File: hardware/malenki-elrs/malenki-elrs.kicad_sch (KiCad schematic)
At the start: 34 parts, among them J1 Conn_01x02_Male-Connector, J2 PROG Header, J3 Weapons, U1 SPX3819M5-L-3-3, U2 ESP32-C3FH4, Y1 ECS-400-10-37B2-CKY-TR

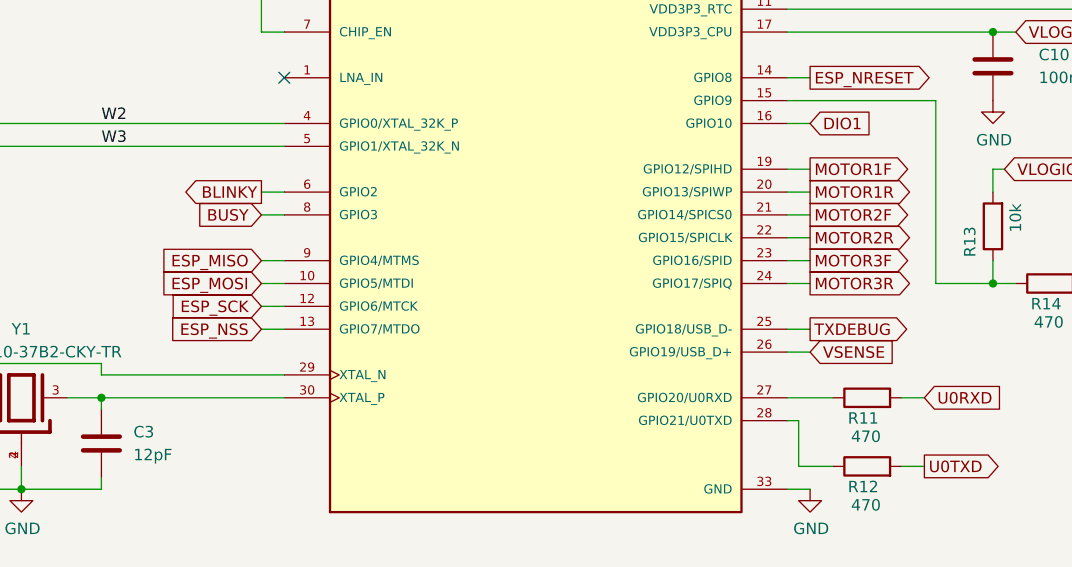
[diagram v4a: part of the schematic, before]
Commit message: Adding ESP32-U4WDH
Found that not enough pins were usable on the esp32-c4 as the internal flash memory still using the SPI bus pins available which I did not initially know about :(
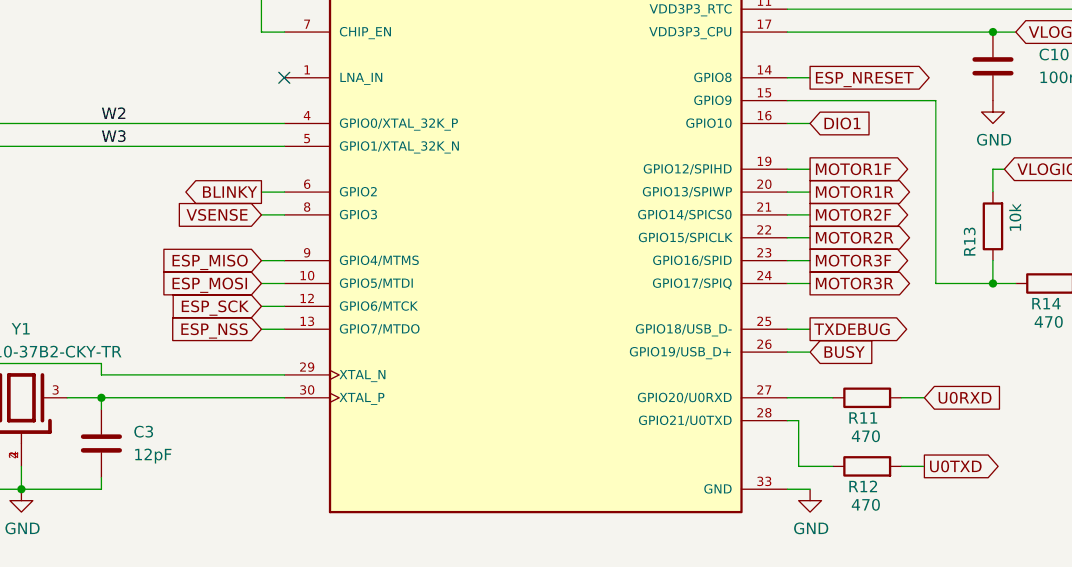
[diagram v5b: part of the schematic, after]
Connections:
- net BUSY: now also U2.26 (GPIO19/USB_D+); no longer U2.8 (GPIO3)
- net VSENSE: now also U2.8 (GPIO3); no longer U2.26 (GPIO19/USB_D+)
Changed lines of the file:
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@@
-	(wire
-		(pts
-			(xy 158.75 119.38) (xy 156.21 119.38)
-		)
-		(stroke
-			(width 0)
-			(type default)
-		)
-	)
 	(wire
 		(pts
@@
 	(wire
 		(pts
+			(xy 242.57 80.01) (xy 245.11 80.01)
+		)
+		(stroke
+			(width 0)
+			(type solid)
+		)
+	)
+	(wire
+		(pts
+			(xy 156.21 101.6) (xy 158.75 101.6)
+		)
+		(stroke
+			(width 0)
+			(type default)
+		)
+	)
+	(wire
+		(pts
+			(xy 125.73 176.53) (xy 125.73 177.8)
+		)
+		(stroke
+			(width 0)
+			(type default)
+		)
+	)
+	(wire
+		(pts
+			(xy 156.21 81.28) (xy 194.31 81.28)
+		)
+		(stroke
+			(width 0)
+			(type default)
+		)
+	)
+	(wire
+		(pts
+			(xy 156.21 78.74) (xy 176.53 78.74)
+		)
+		(stroke
+			(width 0)
+			(type default)
+		)
+	)
+	(wire
+		(pts
+			(xy 97.79 83.82) (xy 100.33 83.82)
+		)
+		(stroke
+			(width 0)
+			(type default)
+		)
+	)
+	(wire
+		(pts
+			(xy 242.57 134.62) (xy 245.11 134.62)
+		)
+		(stroke
+			(width 0)
+			(type solid)
+		)
+	)
+	(wire
+		(pts
+			(xy 59.69 77.47) (xy 64.77 77.47)
+		)
+		(stroke
+			(width 0)
+			(type default)
+		)
+	)
+	(wire
+		(pts
+			(xy 172.72 91.44) (xy 172.72 111.76)
+		)
+		(stroke
+			(width 0)
+			(type default)
+		)
+	)
+	(wire
+		(pts
+			(xy 97.79 101.6) (xy 100.33 101.6)
+		)
+		(stroke
+			(width 0)
+			(type default)
+		)
+	)
+	(wire
+		(pts
+			(xy 176.53 78.74) (xy 176.53 66.04)
+		)
+		(stroke
+			(width 0)
+			(type default)
+		)
+	)
+	(wire
+		(pts
+			(xy 86.36 50.8) (xy 85.09 50.8)
+		)
+		(stroke
+			(width 0)
+			(type default)
+		)
+	)
+	(wire
+		(pts
 			(xy 97.79 104.14) (xy 100.33 104.14)
 		)
@@
 	(wire
 		(pts
-			(xy 242.57 80.01) (xy 245.11 80.01)
-		)
-		(stroke
-			(width 0)
-			(type solid)
-		)
-	)
-	(wire
-		(pts
-			(xy 156.21 101.6) (xy 158.75 101.6)
-		)
-		(stroke
-			(width 0)
-			(type default)
-		)
-	)
-	(wire
-		(pts
-			(xy 125.73 176.53) (xy 125.73 177.8)
-		)
-		(stroke
-			(width 0)
-			(type default)
-		)
-	)
-	(wire
-		(pts
-			(xy 156.21 81.28) (xy 194.31 81.28)
-		)
-		(stroke
-			(width 0)
-			(type default)
-		)
-	)
-	(wire
-		(pts
-			(xy 156.21 78.74) (xy 176.53 78.74)
-		)
-		(stroke
-			(width 0)
-			(type default)
-		)
-	)
-	(wire
-		(pts
-			(xy 97.79 83.82) (xy 100.33 83.82)
-		)
-		(stroke
-			(width 0)
-			(type default)
-		)
-	)
-	(wire
-		(pts
-			(xy 242.57 134.62) (xy 245.11 134.62)
-		)
-		(stroke
-			(width 0)
-			(type solid)
-		)
-	)
-	(wire
-		(pts
-			(xy 59.69 77.47) (xy 64.77 77.47)
-		)
-		(stroke
-			(width 0)
-			(type default)
-		)
-	)
-	(wire
-		(pts
-			(xy 172.72 91.44) (xy 172.72 111.76)
-		)
-		(stroke
-			(width 0)
-			(type default)
-		)
-	)
-	(wire
-		(pts
-			(xy 97.79 101.6) (xy 100.33 101.6)
-		)
-		(stroke
-			(width 0)
-			(type default)
-		)
-	)
-	(wire
-		(pts
-			(xy 176.53 78.74) (xy 176.53 66.04)
-		)
-		(stroke
-			(width 0)
-			(type default)
-		)
-	)
-	(wire
-		(pts
-			(xy 86.36 50.8) (xy 85.09 50.8)
-		)
-		(stroke
-			(width 0)
-			(type default)
-		)
-	)
-	(wire
-		(pts
 			(xy 67.31 93.98) (xy 100.33 93.98)
 		)
@@
 		(pts
 			(xy 99.06 38.1) (xy 104.14 38.1)
+		)
+		(stroke
+			(width 0)
+			(type default)
+		)
+	)
+	(wire
+		(pts
+			(xy 156.21 119.38) (xy 158.75 119.38)
 		)
 		(stroke
@@
 	(global_label "VSENSE"
 		(shape input)
+		(at 97.79 104.14 180)
+		(effects
+			(font
+				(size 1.27 1.27)
+			)
+			(justify right)
+		)
+		(property "Intersheetrefs" "${INTERSHEET_REFS}"
+			(at -13.97 218.44 0)
+			(hide yes)
+			(show_name no)
+			(do_not_autoplace no)
+			(effects
+				(font
+					(size 1.27 1.27)
+				)
+				(justify right)
+			)
+		)
+	)
+	(global_label "BUSY"
+		(shape input)
 		(at 158.75 119.38 0)
-		(effects
-			(font
-				(size 1.27 1.27)
-			)
-			(justify left)
-		)
-		(property "Intersheetrefs" "${INTERSHEET_REFS}"
-			(at 270.51 5.08 0)
-			(hide yes)
-			(show_name no)
-			(do_not_autoplace no)
-			(effects
-				(font
-					(size 1.27 1.27)
-				)
-				(justify left)
-			)
-		)
-	)
-	(global_label "BUSY"
-		(shape input)
-		(at 97.79 104.14 180)
-		(fields_autoplaced yes)
-		(effects
-			(font
-				(size 1.27 1.27)
-			)
-			(justify right)
-		)
-		(property "Intersheetrefs" "${INTERSHEET_REFS}"
-			(at 89.8111 104.14 0)
-			(hide yes)
-			(show_name no)
-			(do_not_autoplace no)
-			(effects
-				(font
-					(size 1.27 1.27)
-				)
-				(justify right)
-			)
-		)
+		(fields_autoplaced yes)
+		(effects
+			(font
+				(size 1.27 1.27)
+			)
+			(justify left)
+		)
+		(property "Intersheetrefs" "${INTERSHEET_REFS}"
+			(at 166.7289 119.38 0)
+			(hide yes)
+			(show_name no)
+			(do_not_autoplace no)
+			(effects
+				(font
+					(size 1.27 1.27)
+				)
+				(justify left)
+			)
+		)

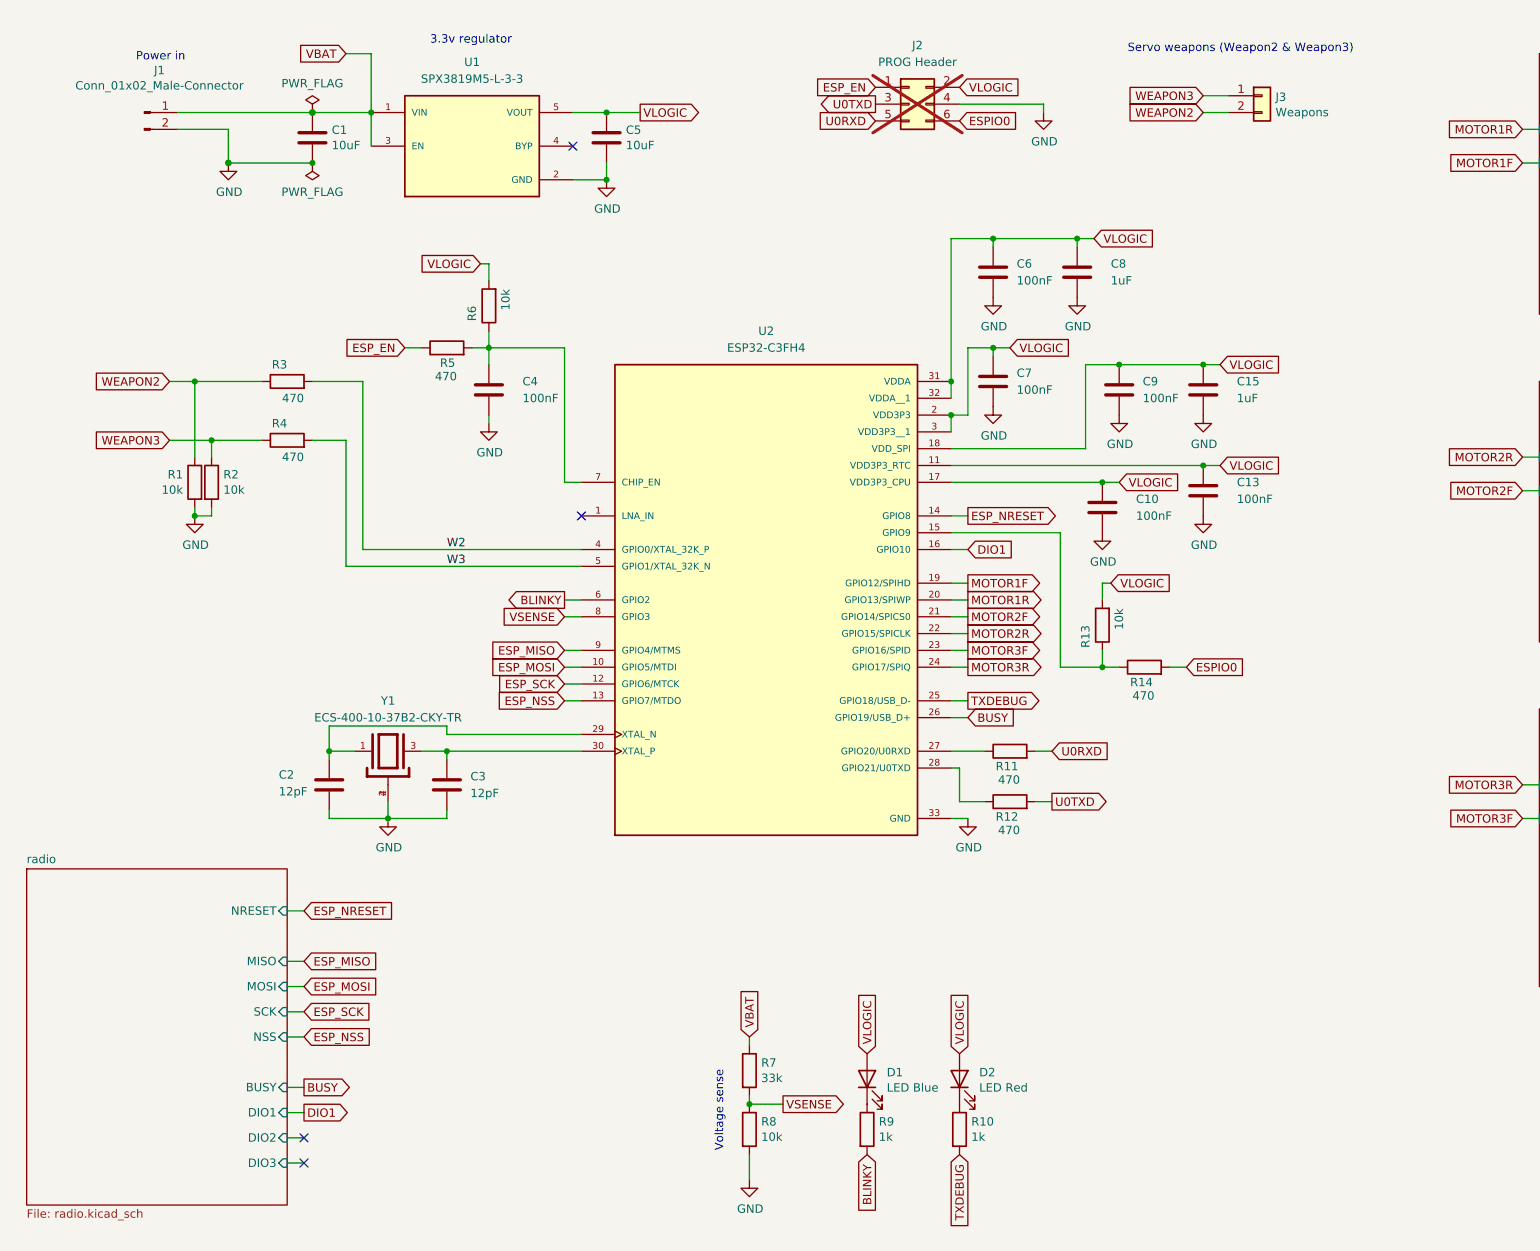
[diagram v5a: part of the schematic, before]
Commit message: Changed microcontroller and completed schematic
Changed micro controller to the esp32-s3FN8, for more available pins.
Complete schematic.
Changed to pcb antenna.
Completed initial placement of all components on PCB.
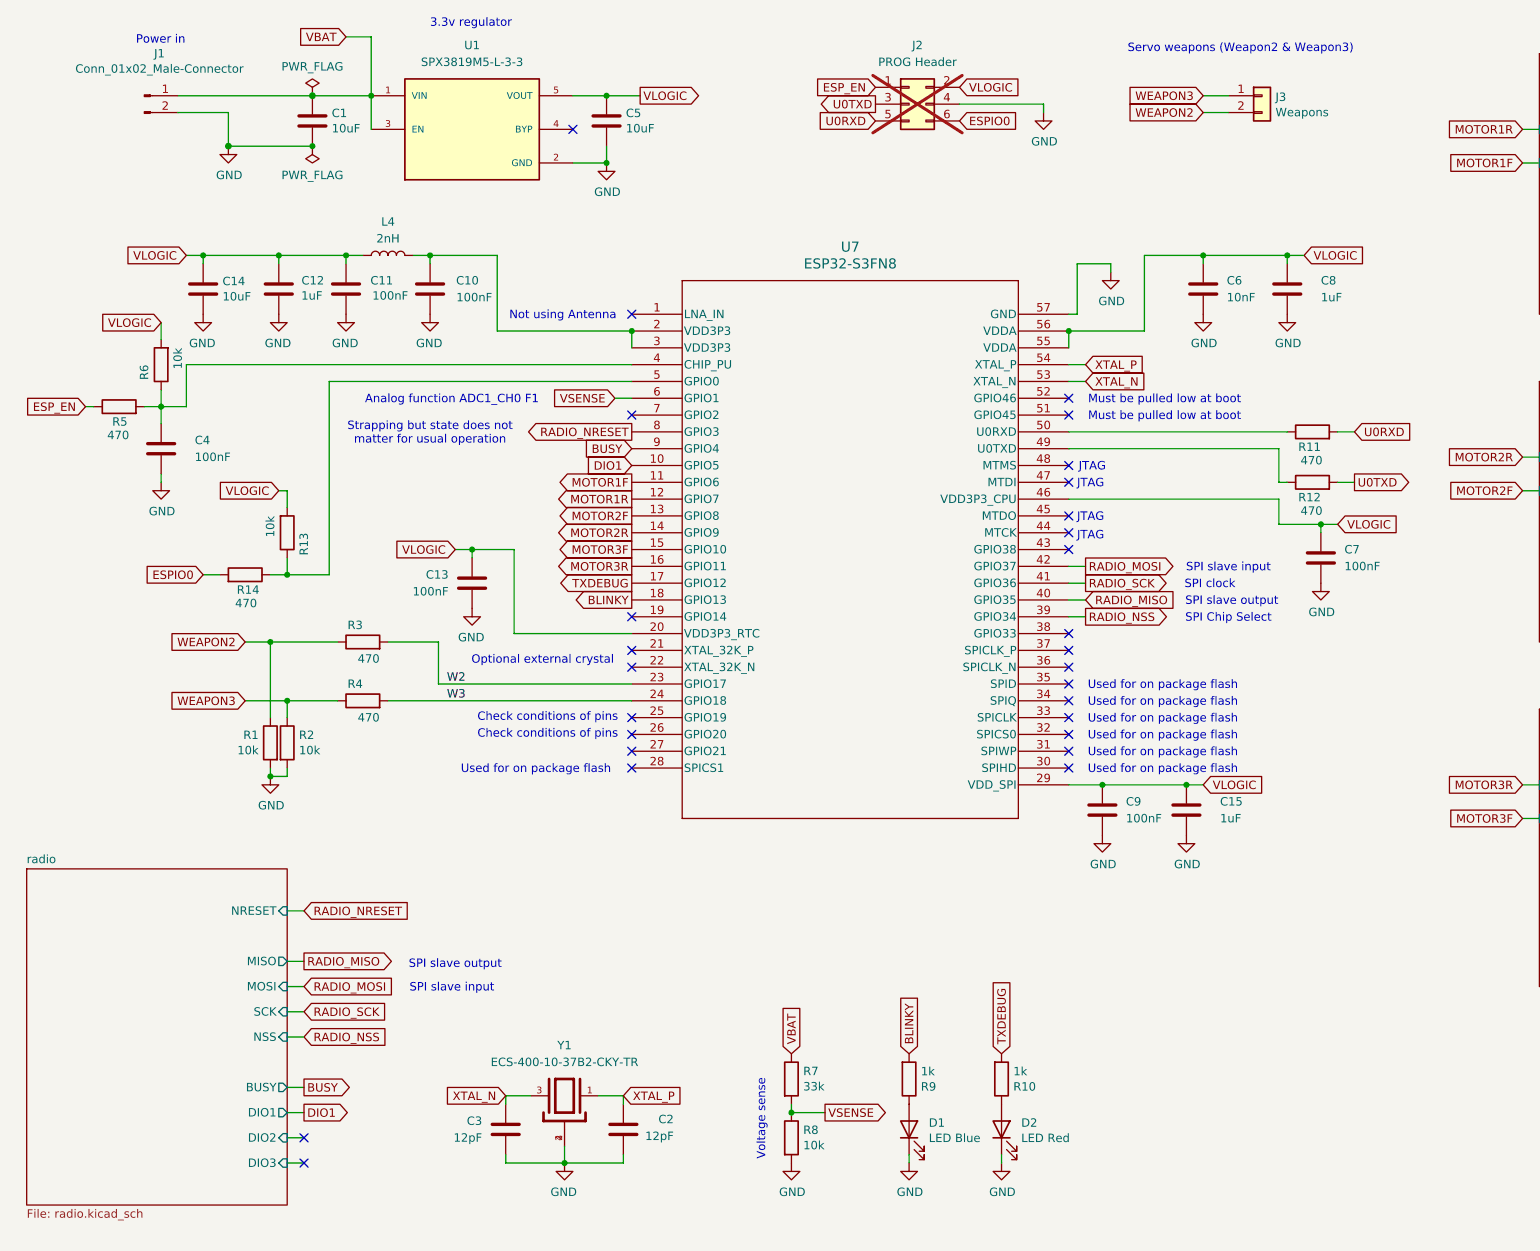
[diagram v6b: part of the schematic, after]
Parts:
- removed U2: ESP32-C3FH4, malenki-nano:QFN50P500X500X90-33N, symbol malenki-elrs:ESP32-C3FH4
- added C11: 100nF, Capacitor_SMD:C_0402_1005Metric, symbol Device:C
- added C12: 1uF, Capacitor_SMD:C_0402_1005Metric, symbol Device:C
- added C14: 10uF, Capacitor_SMD:C_0603_1608Metric, symbol malenki-nano-rescue:C-Device
- added L4: 2nH, Inductor_SMD:L_0402_1005Metric, symbol Device:L
- added U7: ESP32-S3FN8, malenki-nano:QFN56_7X7_EXP, symbol malenki-elrs:ESP32-S3FN8
- C6: value 100nF -> 10nF; LCSC C100072 -> C15195
- D1: footprint LED_SMD:LED_0603_1608Metric -> LED_SMD:LED_0402_1005Metric; LCSC C2986058 -> C22355736; MPN 19-217/BHC-ZL1M2RY/6T -> XL-1005UBC; Manufacturer Everlight -> XINGLIGHT
- D2: footprint LED_SMD:LED_0603_1608Metric -> LED_SMD:LED_0402_1005Metric; LCSC C2986060 -> C25503345; MPN 19-217/R6C-AL1M2VY/6T -> XL-1005SURC; Manufacturer EVERLIGHT -> XINGLIGHT
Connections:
- net BLINKY: now also U7.18 (GPIO13)
- net BUSY: now also U7.9 (GPIO4)
- net DIO1: now also U7.10 (GPIO5)
- net GND: now also D1.1 (K), D2.1 (K), C11.2, C12.2, C14.2, U7.57 (GND)
- net MOTOR1F: now also U7.11 (GPIO6)
- net MOTOR1R: now also U7.12 (GPIO7)
- net MOTOR2F: now also U7.13 (GPIO8)
- net MOTOR2R: now also U7.14 (GPIO9)
- net MOTOR3F: now also U7.15 (GPIO10)
- net MOTOR3R: now also U7.16 (GPIO11)
- net TXDEBUG: now also U7.17 (GPIO12)
- net VLOGIC: now also C11.1, C12.1, C14.1, L4.1, U7.20 (VDD3P3_RTC), U7.29 (VDD_SPI), U7.46 (VDD3P3_CPU), U7.55 (VDDA), U7.56 (VDDA); no longer C10.1, D1.2 (A), D2.2 (A)
- net VSENSE: now also U7.6 (GPIO1)
- net W2: now also U7.23 (GPIO17)
- net W3: now also U7.24 (GPIO18)
- net at R11.1: now also U7.50 (U0RXD)
- net at R10.1: now also D2.2 (A); no longer D2.1 (K)
- net at C4.1, R5.2, R6.1: now also U7.4 (CHIP_PU)
- net XTAL_P: now reaches C2.1, Y1.1
- net XTAL_P: now also U7.54 (XTAL_P)
- net XTAL_N: now reaches C3.1, Y1.3
- net XTAL_N: now also U7.53 (XTAL_N)
- net at R12.1: now also U7.49 (U0TXD)
- net at R9.1: now also D1.2 (A); no longer D1.1 (K)
- net at R13.1, R14.1: now also U7.5 (GPIO0)
- new net: C10.1, L4.2, U7.2 (VDD3P3), U7.3 (VDD3P3)
- new net RADIO_MISO: U7.40 (GPIO35)
- new net RADIO_MOSI: U7.42 (GPIO37)
- new net RADIO_NRESET: U7.8 (GPIO3)
- new net RADIO_NSS: U7.39 (GPIO34)
- new net RADIO_SCK: U7.41 (GPIO36)
- no-connect marks 4 -> 28
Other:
- note added: "Analog function ADC1_CH0 F1"
- note added: "Check conditions of pins"
- note added: "JTAG"
- note added: "Must be pulled low at boot"
- note added: "Not using Antenna"
- note added: "Optional external crystal"
- note added: "SPI Chip Select"
- note added: "SPI clock"
- note added: "SPI slave input"
- note added: "SPI slave output"
- note added: "Strapping but state does not matter for usual operation"
- note added: "Used for on package flash"
- moved on the sheet: C1, C10, C15, C2, C3, C4, C5, C6, C7, C8, C9, D1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

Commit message: Changed component parts to match JLCPCB basic parts
Saving assembly cost by changing all possible components to JLCPCB basic part, and reducing number of separate components where possible. Started trace placement
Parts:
- C10, C11, C13, C4, C7, C9: LCSC C100072 -> C1525; MPN (none) -> CL05B104KO5NNNC
- C12, C15, C8: LCSC C29266 -> C52923; MPN (none) -> CL05A105KA5NQNC
- C2, C3: LCSC C76948 -> C1547; MPN (none) -> 0402CG120J500NT
- R1, R2, R8: LCSC C71617 -> C25744; Manufacturer VISHAY -> (none); Partnum CRCW040210K0FKED -> 0402WGF1002TCE
- R10, R9: value 1k -> 470; LCSC C11702 -> C25117; Manufacturer Uniroyal -> (none); Partnum (none) -> 0402WGF4700TCE
- R11, R12, R14, R4, R5: Partnum (none) -> 0402WGF4700TCE
- R13, R6: LCSC C71617 -> C25744; Partnum CRCW040210K0FKED -> 0402WGF1002TCE
- R7: Manufacturer Uniroyal -> (none); Partnum (none) -> 0402WGF3302TCE

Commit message: Completed trace placement
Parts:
- removed D1: LED Blue, LED_SMD:LED_0402_1005Metric, symbol Device:LED
- removed R9: 470, Resistor_SMD:R_0402_1005Metric, symbol malenki-nano-rescue:R-Device
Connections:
- net BLINKY: no longer names the net of U7.18 (GPIO13)
- no-connect marks 28 -> 29
